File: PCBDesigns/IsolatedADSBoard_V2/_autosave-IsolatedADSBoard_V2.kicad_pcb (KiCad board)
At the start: 4 copper layers, 21.6 x 41.4 mm, 20 parts, among them J1 Screw_Terminal_01x06, J2 Screw_Terminal_01x08, J3 Conn_01x04_MountingPin, J4 Conn_01x04_MountingPin, J5 Conn_01x04_MountingPin, U1 ADuM1200AR, U13 ISO1540, U14 RFM-0505S, U3 ADS1115IDGS

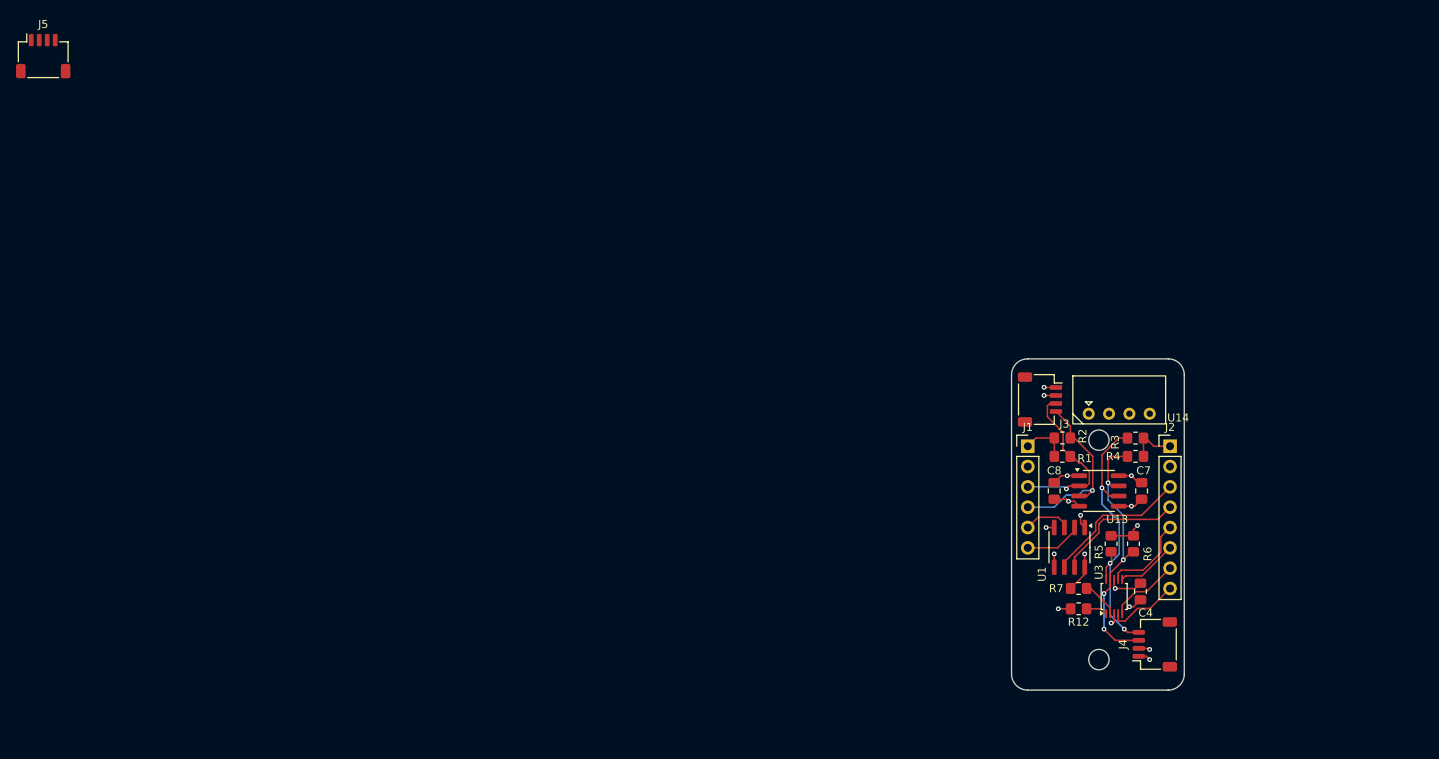
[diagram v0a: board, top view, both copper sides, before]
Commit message: Some radio work. Adding circuit disable to open lead detect proof.
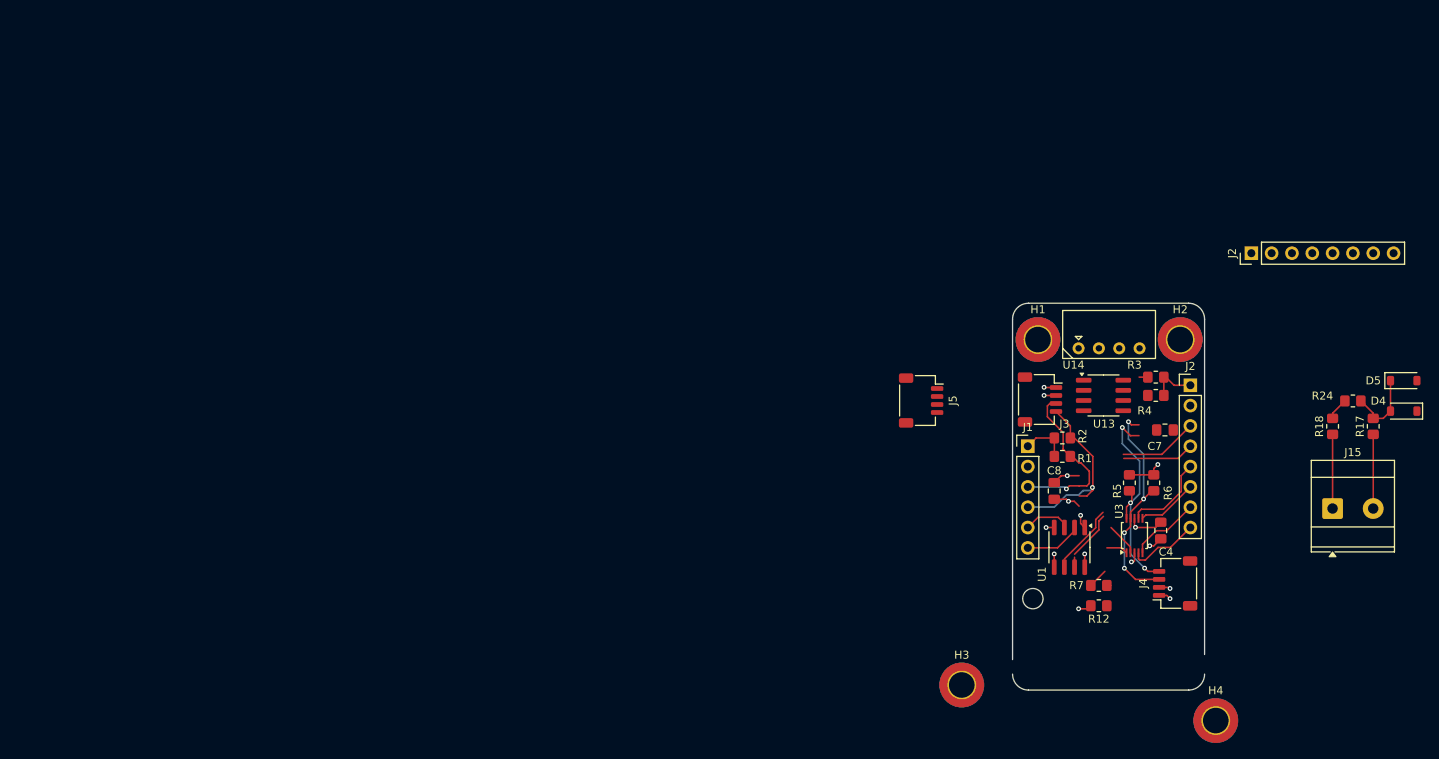
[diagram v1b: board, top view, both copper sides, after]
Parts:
- added D4: D_Schottky, Diode_SMD:D_SOD-123, F.Cu at (174.0, 47.7)
- added D5: D_Schottky, Diode_SMD:D_SOD-123, F.Cu at (174.0, 43.9)
- added H1: MountingHole, MountingHole:MountingHole_3.2mm_M3_DIN965_Pad_TopBottom, F.Cu at (128.3, 38.7)
- added H2: MountingHole, MountingHole:MountingHole_3.2mm_M3_DIN965_Pad_TopBottom, F.Cu at (146.1, 38.7)
- added H3: MountingHole, MountingHole:MountingHole_3.2mm_M3_DIN965_Pad_TopBottom, F.Cu at (118.7, 81.9)
- added H4: MountingHole, MountingHole:MountingHole_3.2mm_M3_DIN965_Pad_TopBottom, F.Cu at (150.5, 86.4)
- added J15: Barrel_Jack, TerminalBlock_Phoenix:TerminalBlock_Phoenix_MKDS-3-2-5.08_1x02_P5.08mm_Horizontal, F.Cu at (165.1, 59.9)
- added J2: Screw_Terminal_01x08, Connector_PinHeader_2.54mm:PinHeader_1x08_P2.54mm_Vertical, F.Cu at (154.9, 27.9)
- added R17: 499.0K, Resistor_SMD:R_0805_2012Metric_Pad1.20x1.40mm_HandSolder, F.Cu at (170.2, 49.6)
- added R18: 499.0K, Resistor_SMD:R_0805_2012Metric_Pad1.20x1.40mm_HandSolder, F.Cu at (165.1, 49.6)
- added R24: 15K, Resistor_SMD:R_0805_2012Metric_Pad1.20x1.40mm_HandSolder, F.Cu at (167.6, 46.4)
- moved J5 117.9 mm to (113.7, 46.4), turned to -90 degrees
- moved U13 12.0 mm to (136.5, 45.7)
- moved U14 8.27 mm to (138.5, 38.7)
- moved C7 8.16 mm to (144.1, 50.0), turned to 0 degrees
- moved R3 8.03 mm to (143.0, 43.4)
- moved R4 8.03 mm to (143.0, 45.7)
- moved U3 8.03 mm to (140.3, 63.2)
- moved C4 8.03 mm to (143.6, 62.6)
- moved J2 8.03 mm to (147.3, 44.5)
- moved R6 8.03 mm to (142.7, 56.6)
- moved J4 8.03 mm to (145.4, 69.2)
- moved R5 7.96 mm to (139.7, 56.6)
- moved R12 2.56 mm to (135.9, 72.0)
- moved R7 2.56 mm to (135.9, 69.5)
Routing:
- net Net-(J15-Pin_1): track 0.00 -> 9.33 mm
- net Net-(J15-Pin_2): track 0.00 -> 9.33 mm
- net /AIN3: track 10.8 -> 19.9 mm
- net SCL-5V: track 36.2 -> 29.1 mm
- net SDA-5V: track 33.7 -> 28.2 mm
- net 5V-iso: track 24.6 -> 21.4 mm, vias 5 -> 4
- net Gnd-iso: track 11.2 -> 7.94 mm, vias 6 -> 5
- net /AIN2: track 7.61 -> 10.4 mm
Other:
- board size 21.6 x 41.4 mm -> 24 x 48.4 mm
